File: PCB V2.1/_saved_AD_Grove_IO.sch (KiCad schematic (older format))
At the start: 12 parts, among them J13 S4B-PH-SM4-TB(LF)(SN), J14 S4B-PH-SM4-TB(LF)(SN), J15 S4B-PH-SM4-TB(LF)(SN), J16 S4B-PH-SM4-TB(LF)(SN)

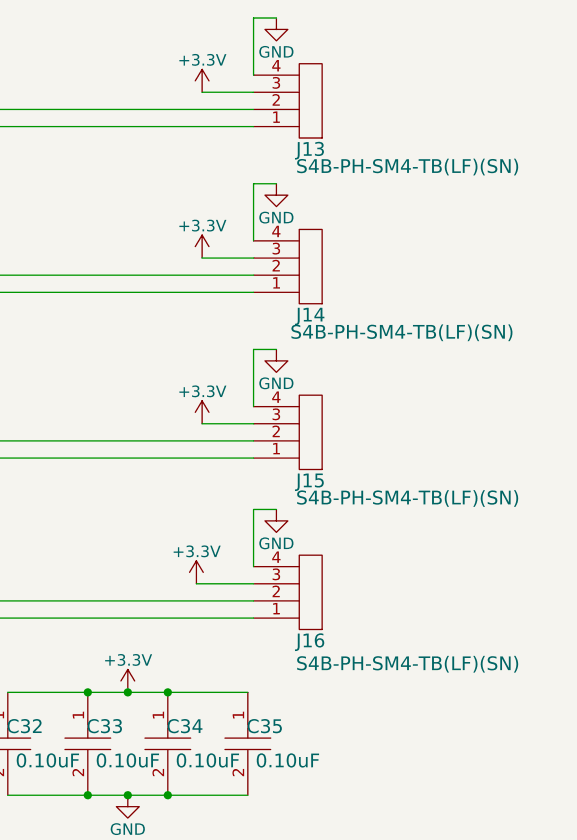
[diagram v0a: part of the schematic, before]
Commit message: Revert "Placement near completeq"
This reverts commit ae7bce2a0b52adb9ec10d03d9117548a28df5835.
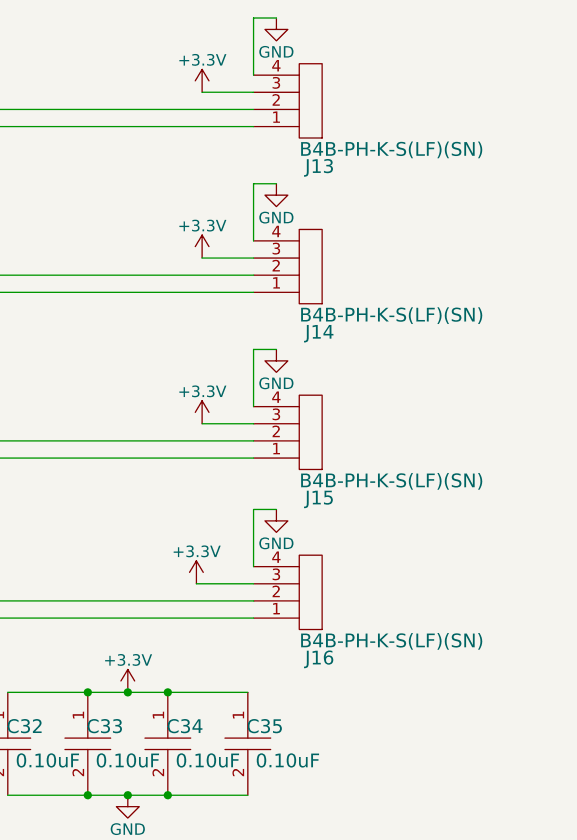
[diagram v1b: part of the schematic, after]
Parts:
- removed J13, J14, J15, J16: S4B-PH-SM4-TB(LF)(SN), PCB_Footprints:S4B-PH-SM4-TB(LF)(SN), symbol S4B-PH-SM4-TB(LF)(SN)
- added J13, J14, J15, J16: B4B-PH-K-S(LF)(SN), PCB_Footprints:B4B-PH-K-S(LF)(SN), symbol B4B-PH-K-S(LF)(SN)
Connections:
- net +3V3: now also J13.3, J14.3, J15.3, J16.3
- net ANIO_0: now also J13.2
- net ANIO_1: now also J13.1
- net ANIO_2: now also J14.2
- net ANIO_3: now also J14.1
- net ANIO_4: now also J15.2
- net ANIO_5: now also J15.1
- net ANIO_6: now also J16.2
- net ANIO_7: now also J16.1
- net GND: now also J13.4, J14.4, J15.4, J16.4
